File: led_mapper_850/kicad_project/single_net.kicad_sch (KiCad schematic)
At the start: 530 parts, among them J1 Conn_02x12_Top_Bottom

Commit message: use single connector
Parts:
- removed J1: Conn_02x12_Top_Bottom, ccatlib:PinSocket_2x12_P2.54mm_Vertical_SMD_custom, symbol Connector_Generic:Conn_02x12_Top_Bottom
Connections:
- net P01: no longer D1.2 (A), D139.2 (A), D185.2 (A), D231.2 (A), D277.2 (A), D323.2 (A), D369.2 (A), D415.2 (A), D461.2 (A), D47.2 (A), D507.2 (A), D93.2 (A)
- net P02: no longer D140.2 (A), D186.2 (A), D2.2 (A), D232.2 (A), D278.2 (A), D324.2 (A), D370.2 (A), D416.2 (A), D462.2 (A), D48.2 (A), D484.1 (K), D485.1 (K), D486.1 (K), D487.1 (K), D488.1 (K), D489.1 (K), D490.1 (K), D491.1 (K), D492.1 (K), D493.1 (K), D494.1 (K), D495.1 (K), D496.1 (K), D497.1 (K), D498.1 (K), D499.1 (K), D500.1 (K), D501.1 (K), D502.1 (K), D503.1 (K), D504.1 (K), D505.1 (K), D506.1 (K), D508.2 (A), D94.2 (A)
- net P03: no longer D141.2 (A), D187.2 (A), D233.2 (A), D279.2 (A), D3.2 (A), D325.2 (A), D371.2 (A), D417.2 (A), D438.1 (K), D439.1 (K), D440.1 (K), D441.1 (K), D442.1 (K), D443.1 (K), D444.1 (K), D445.1 (K), D446.1 (K), D447.1 (K), D448.1 (K), D449.1 (K), D450.1 (K), D451.1 (K), D452.1 (K), D453.1 (K), D454.1 (K), D455.1 (K), D456.1 (K), D457.1 (K), D458.1 (K), D459.1 (K), D460.1 (K), D463.2 (A), D49.2 (A), D509.2 (A), D95.2 (A)
- net P04: no longer D142.2 (A), D188.2 (A), D234.2 (A), D280.2 (A), D326.2 (A), D372.2 (A), D392.1 (K), D393.1 (K), D394.1 (K), D395.1 (K), D396.1 (K), D397.1 (K), D398.1 (K), D399.1 (K), D4.2 (A), D400.1 (K), D401.1 (K), D402.1 (K), D403.1 (K), D404.1 (K), D405.1 (K), D406.1 (K), D407.1 (K), D408.1 (K), D409.1 (K), D410.1 (K), D411.1 (K), D412.1 (K), D413.1 (K), D414.1 (K), D418.2 (A), D464.2 (A), D50.2 (A), D510.2 (A), D96.2 (A)
- net P05: no longer D143.2 (A), D189.2 (A), D235.2 (A), D281.2 (A), D327.2 (A), D346.1 (K), D347.1 (K), D348.1 (K), D349.1 (K), D350.1 (K), D351.1 (K), D352.1 (K), D353.1 (K), D354.1 (K), D355.1 (K), D356.1 (K), D357.1 (K), D358.1 (K), D359.1 (K), D360.1 (K), D361.1 (K), D362.1 (K), D363.1 (K), D364.1 (K), D365.1 (K), D366.1 (K), D367.1 (K), D368.1 (K), D373.2 (A), D419.2 (A), D465.2 (A), D5.2 (A), D51.2 (A), D511.2 (A), D97.2 (A)
- net P06: no longer D144.2 (A), D190.2 (A), D236.2 (A), D282.2 (A), D300.1 (K), D301.1 (K), D302.1 (K), D303.1 (K), D304.1 (K), D305.1 (K), D306.1 (K), D307.1 (K), D308.1 (K), D309.1 (K), D310.1 (K), D311.1 (K), D312.1 (K), D313.1 (K), D314.1 (K), D315.1 (K), D316.1 (K), D317.1 (K), D318.1 (K), D319.1 (K), D320.1 (K), D321.1 (K), D322.1 (K), D328.2 (A), D374.2 (A), D420.2 (A), D466.2 (A), D512.2 (A), D52.2 (A), D6.2 (A), D98.2 (A)
- net P07: no longer D145.2 (A), D191.2 (A), D237.2 (A), D254.1 (K), D255.1 (K), D256.1 (K), D257.1 (K), D258.1 (K), D259.1 (K), D260.1 (K), D261.1 (K), D262.1 (K), D263.1 (K), D264.1 (K), D265.1 (K), D266.1 (K), D267.1 (K), D268.1 (K), D269.1 (K), D270.1 (K), D271.1 (K), D272.1 (K), D273.1 (K), D274.1 (K), D275.1 (K), D276.1 (K), D283.2 (A), D329.2 (A), D375.2 (A), D421.2 (A), D467.2 (A), D513.2 (A), D53.2 (A), D7.2 (A), D99.2 (A)
- net P08: no longer D100.2 (A), D146.2 (A), D192.2 (A), D208.1 (K), D209.1 (K), D210.1 (K), D211.1 (K), D212.1 (K), D213.1 (K), D214.1 (K), D215.1 (K), D216.1 (K), D217.1 (K), D218.1 (K), D219.1 (K), D220.1 (K), D221.1 (K), D222.1 (K), D223.1 (K), D224.1 (K), D225.1 (K), D226.1 (K), D227.1 (K), D228.1 (K), D229.1 (K), D230.1 (K), D238.2 (A), D284.2 (A), D330.2 (A), D376.2 (A), D422.2 (A), D468.2 (A), D514.2 (A), D54.2 (A), D8.2 (A)
- net P09: no longer D101.2 (A), D147.2 (A), D162.1 (K), D163.1 (K), D164.1 (K), D165.1 (K), D166.1 (K), D167.1 (K), D168.1 (K), D169.1 (K), D170.1 (K), D171.1 (K), D172.1 (K), D173.1 (K), D174.1 (K), D175.1 (K), D176.1 (K), D177.1 (K), D178.1 (K), D179.1 (K), D180.1 (K), D181.1 (K), D182.1 (K), D183.1 (K), D184.1 (K), D193.2 (A), D239.2 (A), D285.2 (A), D331.2 (A), D377.2 (A), D423.2 (A), D469.2 (A), D515.2 (A), D55.2 (A), D9.2 (A)
- new net P1: D1.2 (A), D139.2 (A), D185.2 (A), D231.2 (A), D277.2 (A), D323.2 (A), D369.2 (A), D415.2 (A), D461.2 (A), D47.2 (A), D507.2 (A), D93.2 (A)
- new net P2: D140.2 (A), D186.2 (A), D2.2 (A), D232.2 (A), D278.2 (A), D324.2 (A), D370.2 (A), D416.2 (A), D462.2 (A), D48.2 (A), D484.1 (K), D485.1 (K), D486.1 (K), D487.1 (K), D488.1 (K), D489.1 (K), D490.1 (K), D491.1 (K), D492.1 (K), D493.1 (K), D494.1 (K), D495.1 (K), D496.1 (K), D497.1 (K), D498.1 (K), D499.1 (K), D500.1 (K), D501.1 (K), D502.1 (K), D503.1 (K), D504.1 (K), D505.1 (K), D506.1 (K), D508.2 (A), D94.2 (A)
- new net P3: D141.2 (A), D187.2 (A), D233.2 (A), D279.2 (A), D3.2 (A), D325.2 (A), D371.2 (A), D417.2 (A), D438.1 (K), D439.1 (K), D440.1 (K), D441.1 (K), D442.1 (K), D443.1 (K), D444.1 (K), D445.1 (K), D446.1 (K), D447.1 (K), D448.1 (K), D449.1 (K), D450.1 (K), D451.1 (K), D452.1 (K), D453.1 (K), D454.1 (K), D455.1 (K), D456.1 (K), D457.1 (K), D458.1 (K), D459.1 (K), D460.1 (K), D463.2 (A), D49.2 (A), D509.2 (A), D95.2 (A)
- new net P4: D142.2 (A), D188.2 (A), D234.2 (A), D280.2 (A), D326.2 (A), D372.2 (A), D392.1 (K), D393.1 (K), D394.1 (K), D395.1 (K), D396.1 (K), D397.1 (K), D398.1 (K), D399.1 (K), D4.2 (A), D400.1 (K), D401.1 (K), D402.1 (K), D403.1 (K), D404.1 (K), D405.1 (K), D406.1 (K), D407.1 (K), D408.1 (K), D409.1 (K), D410.1 (K), D411.1 (K), D412.1 (K), D413.1 (K), D414.1 (K), D418.2 (A), D464.2 (A), D50.2 (A), D510.2 (A), D96.2 (A)
- new net P5: D143.2 (A), D189.2 (A), D235.2 (A), D281.2 (A), D327.2 (A), D346.1 (K), D347.1 (K), D348.1 (K), D349.1 (K), D350.1 (K), D351.1 (K), D352.1 (K), D353.1 (K), D354.1 (K), D355.1 (K), D356.1 (K), D357.1 (K), D358.1 (K), D359.1 (K), D360.1 (K), D361.1 (K), D362.1 (K), D363.1 (K), D364.1 (K), D365.1 (K), D366.1 (K), D367.1 (K), D368.1 (K), D373.2 (A), D419.2 (A), D465.2 (A), D5.2 (A), D51.2 (A), D511.2 (A), D97.2 (A)
- new net P6: D144.2 (A), D190.2 (A), D236.2 (A), D282.2 (A), D300.1 (K), D301.1 (K), D302.1 (K), D303.1 (K), D304.1 (K), D305.1 (K), D306.1 (K), D307.1 (K), D308.1 (K), D309.1 (K), D310.1 (K), D311.1 (K), D312.1 (K), D313.1 (K), D314.1 (K), D315.1 (K), D316.1 (K), D317.1 (K), D318.1 (K), D319.1 (K), D320.1 (K), D321.1 (K), D322.1 (K), D328.2 (A), D374.2 (A), D420.2 (A), D466.2 (A), D512.2 (A), D52.2 (A), D6.2 (A), D98.2 (A)
- new net P7: D145.2 (A), D191.2 (A), D237.2 (A), D254.1 (K), D255.1 (K), D256.1 (K), D257.1 (K), D258.1 (K), D259.1 (K), D260.1 (K), D261.1 (K), D262.1 (K), D263.1 (K), D264.1 (K), D265.1 (K), D266.1 (K), D267.1 (K), D268.1 (K), D269.1 (K), D270.1 (K), D271.1 (K), D272.1 (K), D273.1 (K), D274.1 (K), D275.1 (K), D276.1 (K), D283.2 (A), D329.2 (A), D375.2 (A), D421.2 (A), D467.2 (A), D513.2 (A), D53.2 (A), D7.2 (A), D99.2 (A)
- new net P8: D100.2 (A), D146.2 (A), D192.2 (A), D208.1 (K), D209.1 (K), D210.1 (K), D211.1 (K), D212.1 (K), D213.1 (K), D214.1 (K), D215.1 (K), D216.1 (K), D217.1 (K), D218.1 (K), D219.1 (K), D220.1 (K), D221.1 (K), D222.1 (K), D223.1 (K), D224.1 (K), D225.1 (K), D226.1 (K), D227.1 (K), D228.1 (K), D229.1 (K), D230.1 (K), D238.2 (A), D284.2 (A), D330.2 (A), D376.2 (A), D422.2 (A), D468.2 (A), D514.2 (A), D54.2 (A), D8.2 (A)
- new net P9: D101.2 (A), D147.2 (A), D162.1 (K), D163.1 (K), D164.1 (K), D165.1 (K), D166.1 (K), D167.1 (K), D168.1 (K), D169.1 (K), D170.1 (K), D171.1 (K), D172.1 (K), D173.1 (K), D174.1 (K), D175.1 (K), D176.1 (K), D177.1 (K), D178.1 (K), D179.1 (K), D180.1 (K), D181.1 (K), D182.1 (K), D183.1 (K), D184.1 (K), D193.2 (A), D239.2 (A), D285.2 (A), D331.2 (A), D377.2 (A), D423.2 (A), D469.2 (A), D515.2 (A), D55.2 (A), D9.2 (A)

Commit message: add led part number - XINGLIGHT Red 0201
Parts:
- D1, D10, D100, D101, D102, D103, D104, D105, D106, D107, D108, D109, D11, D110, D111, D112, D113, D114, D115, D116, D117, D118, D119, D12, D120, D121, D122, D123, D124, D125, D126, D127, D128, D129, D13, D130, D131, D132, D133, D134, D135, D136, D137, D138, D139, D14, D140, D141, D142, D143, D144, D145, D146, D147, D148, D149, D15, D150, D151, D152, D153, D154, D155, D156, D157, D158, D159, D16, D160, D161, D162, D163, D164, D165, D166, D167, D168, D169, D17, D170, D171, D172, D173, D174, D175, D176, D177, D178, D179, D18, D180, D181, D182, D183, D184, D185, D186, D187, D188, D189, D19, D190, D191, D192, D193, D194, D195, D196, D197, D198, D199, D2, D20, D200, D201, D202, D203, D204, D205, D206, D207, D208, D209, D21, D210, D211, D212, D213, D214, D215, D216, D217, D218, D219, D22, D220, D221, D222, D223, D224, D225, D226, D227, D228, D229, D23, D230, D231, D232, D233, D234, D235, D236, D237, D238, D239, D24, D240, D241, D242, D243, D244, D245, D246, D247, D248, D249, D25, D250, D251, D252, D253, D254, D255, D256, D257, D258, D259, D26, D260, D261, D262, D263, D264, D265, D266, D267, D268, D269, D27, D270, D271, D272, D273, D274, D275, D276, D277, D278, D279, D28, D280, D281, D282, D283, D284, D285, D286, D287, D288, D289, D29, D290, D291, D292, D293, D294, D295, D296, D297, D298, D299, D3, D30, D300, D301, D302, D303, D304, D305, D306, D307, D308, D309, D31, D310, D311, D312, D313, D314, D315, D316, D317, D318, D319, D32, D320, D321, D322, D323, D324, D325, D326, D327, D328, D329, D33, D330, D331, D332, D333, D334, D335, D336, D337, D338, D339, D34, D340, D341, D342, D343, D344, D345, D346, D347, D348, D349, D35, D350, D351, D352, D353, D354, D355, D356, D357, D358, D359, D36, D360, D361, D362, D363, D364, D365, D366, D367, D368, D369, D37, D370, D371, D372, D373, D374, D375, D376, D377, D378, D379, D38, D380, D381, D382, D383, D384, D385, D386, D387, D388, D389, D39, D390, D391, D392, D393, D394, D395, D396, D397, D398, D399, D4, D40, D400, D401, D402, D403, D404, D405, D406, D407, D408, D409, D41, D410, D411, D412, D413, D414, D415, D416, D417, D418, D419, D42, D420, D421, D422, D423, D424, D425, D426, D427, D428, D429, D43, D430, D431, D432, D433, D434, D435, D436, D437, D438, D439, D44, D440, D441, D442, D443, D444, D445, D446, D447, D448, D449, D45, D450, D451, D452, D453, D454, D455, D456, D457, D458, D459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: LCSC PN (none) -> C3646923

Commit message: add fabrication outputs for previewing PCBA quote
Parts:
- D1, D10, D100, D101, D102, D103, D104, D105, D106, D107, D108, D109, D11, D110, D111, D112, D113, D114, D115, D116, D117, D118, D119, D12, D120, D121, D122, D123, D124, D125, D126, D127, D128, D129, D13, D130, D131, D132, D133, D134, D135, D136, D137, D138, D139, D14, D140, D141, D142, D143, D144, D145, D146, D147, D148, D149, D15, D150, D151, D152, D153, D154, D155, D156, D157, D158, D159, D16, D160, D161, D162, D163, D164, D165, D166, D167, D168, D169, D17, D170, D171, D172, D173, D174, D175, D176, D177, D178, D179, D18, D180, D181, D182, D183, D184, D185, D186, D187, D188, D189, D19, D190, D191, D192, D193, D194, D195, D196, D197, D198, D199, D2, D20, D200, D201, D202, D203, D204, D205, D206, D207, D208, D209, D21, D210, D211, D212, D213, D214, D215, D216, D217, D218, D219, D22, D220, D221, D222, D223, D224, D225, D226, D227, D228, D229, D23, D230, D231, D232, D233, D234, D235, D236, D237, D238, D239, D24, D240, D241, D242, D243, D244, D245, D246, D247, D248, D249, D25, D250, D251, D252, D253, D254, D255, D256, D257, D258, D259, D26, D260, D261, D262, D263, D264, D265, D266, D267, D268, D269, D27, D270, D271, D272, D273, D274, D275, D276, D277, D278, D279, D28, D280, D281, D282, D283, D284, D285, D286, D287, D288, D289, D29, D290, D291, D292, D293, D294, D295, D296, D297, D298, D299, D3, D30, D300, D301, D302, D303, D304, D305, D306, D307, D308, D309, D31, D310, D311, D312, D313, D314, D315, D316, D317, D318, D319, D32, D320, D321, D322, D323, D324, D325, D326, D327, D328, D329, D33, D330, D331, D332, D333, D334, D335, D336, D337, D338, D339, D34, D340, D341, D342, D343, D344, D345, D346, D347, D348, D349, D35, D350, D351, D352, D353, D354, D355, D356, D357, D358, D359, D36, D360, D361, D362, D363, D364, D365, D366, D367, D368, D369, D37, D370, D371, D372, D373, D374, D375, D376, D377, D378, D379, D38, D380, D381, D382, D383, D384, D385, D386, D387, D388, D389, D39, D390, D391, D392, D393, D394, D395, D396, D397, D398, D399, D4, D40, D400, D401, D402, D403, D404, D405, D406, D407, D408, D409, D41, D410, D411, D412, D413, D414, D415, D416, D417, D418, D419, D42, D420, D421, D422, D423, D424, D425, D426, D427, D428, D429, D43, D430, D431, D432, D433, D434, D435, D436, D437, D438, D439, D44, D440, D441, D442, D443, D444, D445, D446, D447, D448, D449, D45, D450, D451, D452, D453, D454, D455, D456, D457, D458, D459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: LCSC PN C3646923 -> (none); LCSC Part # (none) -> C3646923

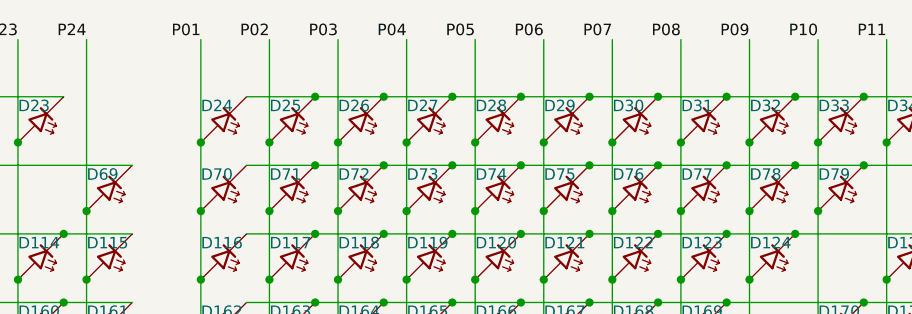
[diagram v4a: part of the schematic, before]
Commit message: fix critical schematic error - wrong pins
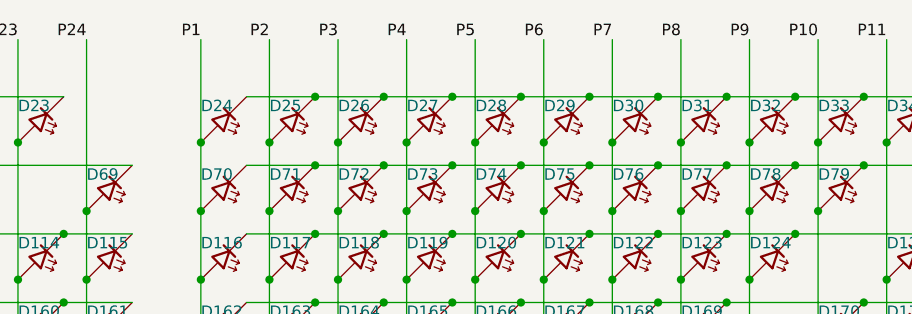
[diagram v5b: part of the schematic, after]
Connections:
- net P01 is gone; now on net P1: D116.2 (A), D162.2 (A), D208.2 (A), D24.2 (A), D254.2 (A), D300.2 (A), D346.2 (A), D392.2 (A), D438.2 (A), D484.2 (A), D70.2 (A)
- net P02 is gone; now on net P2: D117.2 (A), D163.2 (A), D209.2 (A), D25.2 (A), D255.2 (A), D301.2 (A), D347.2 (A), D393.2 (A), D439.2 (A), D71.2 (A)
- net P03 is gone; now on net P3: D118.2 (A), D164.2 (A), D210.2 (A), D256.2 (A), D26.2 (A), D302.2 (A), D348.2 (A), D394.2 (A), D485.2 (A), D72.2 (A)
- net P04 is gone; now on net P4: D119.2 (A), D165.2 (A), D211.2 (A), D257.2 (A), D27.2 (A), D303.2 (A), D349.2 (A), D440.2 (A), D486.2 (A), D73.2 (A)
- net P05 is gone; now on net P5: D120.2 (A), D166.2 (A), D212.2 (A), D258.2 (A), D28.2 (A), D304.2 (A), D395.2 (A), D441.2 (A), D487.2 (A), D74.2 (A)
- net P06 is gone; now on net P6: D121.2 (A), D167.2 (A), D213.2 (A), D259.2 (A), D29.2 (A), D350.2 (A), D396.2 (A), D442.2 (A), D488.2 (A), D75.2 (A)
- net P07 is gone; now on net P7: D122.2 (A), D168.2 (A), D214.2 (A), D30.2 (A), D305.2 (A), D351.2 (A), D397.2 (A), D443.2 (A), D489.2 (A), D76.2 (A)
- net P08 is gone; now on net P8: D123.2 (A), D169.2 (A), D260.2 (A), D306.2 (A), D31.2 (A), D352.2 (A), D398.2 (A), D444.2 (A), D490.2 (A), D77.2 (A)
- net P09 is gone; now on net P9: D124.2 (A), D215.2 (A), D261.2 (A), D307.2 (A), D32.2 (A), D353.2 (A), D399.2 (A), D445.2 (A), D491.2 (A), D78.2 (A)
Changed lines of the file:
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@@
 		)
 	)
-	(label "P03"
+	(label "P3"
 		(at 232.41 20.32 180)
 		(effects
@@
 		)
 	)
-	(label "P04"
+	(label "P4"
 		(at 240.03 20.32 180)
 		(effects
@@
 		)
 	)
-	(label "P07"
+	(label "P7"
 		(at 262.89 20.32 180)
 		(effects
@@
 		)
 	)
-	(label "P08"
+	(label "P8"
 		(at 270.51 20.32 180)
 		(effects
@@
 		)
 	)
-	(label "P05"
+	(label "P5"
 		(at 247.65 20.32 180)
 		(effects
@@
 		)
 	)
-	(label "P09"
+	(label "P9"
 		(at 278.13 20.32 180)
 		(effects
@@
 		)
 	)
-	(label "P02"
+	(label "P2"
 		(at 224.79 20.32 180)
 		(effects
@@
 		)
 	)
-	(label "P01"
+	(label "P1"
 		(at 217.17 20.32 180)
 		(effects
@@
 		)
 	)
-	(label "P06"
+	(label "P6"
 		(at 255.27 20.32 180)
 		(effects
